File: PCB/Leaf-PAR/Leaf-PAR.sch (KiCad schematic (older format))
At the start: 3 parts

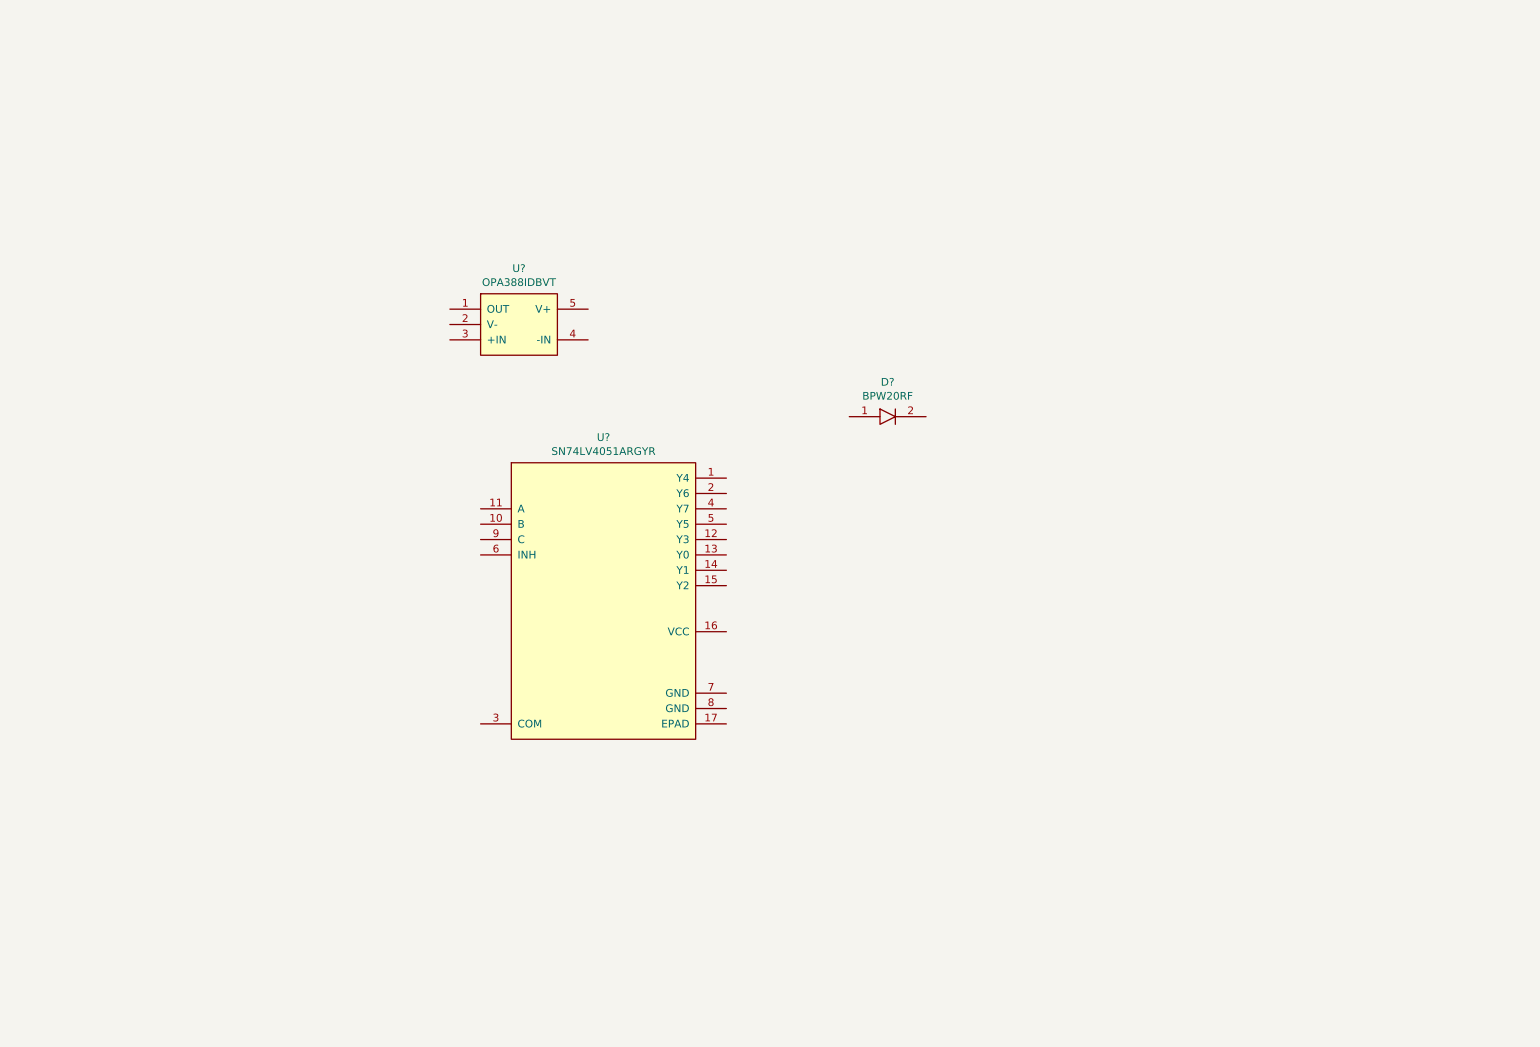
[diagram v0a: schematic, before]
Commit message: Schematic
Schematic pass 1 complete, next to add interface connector, need to decide if ADC or MCU should be integrated.
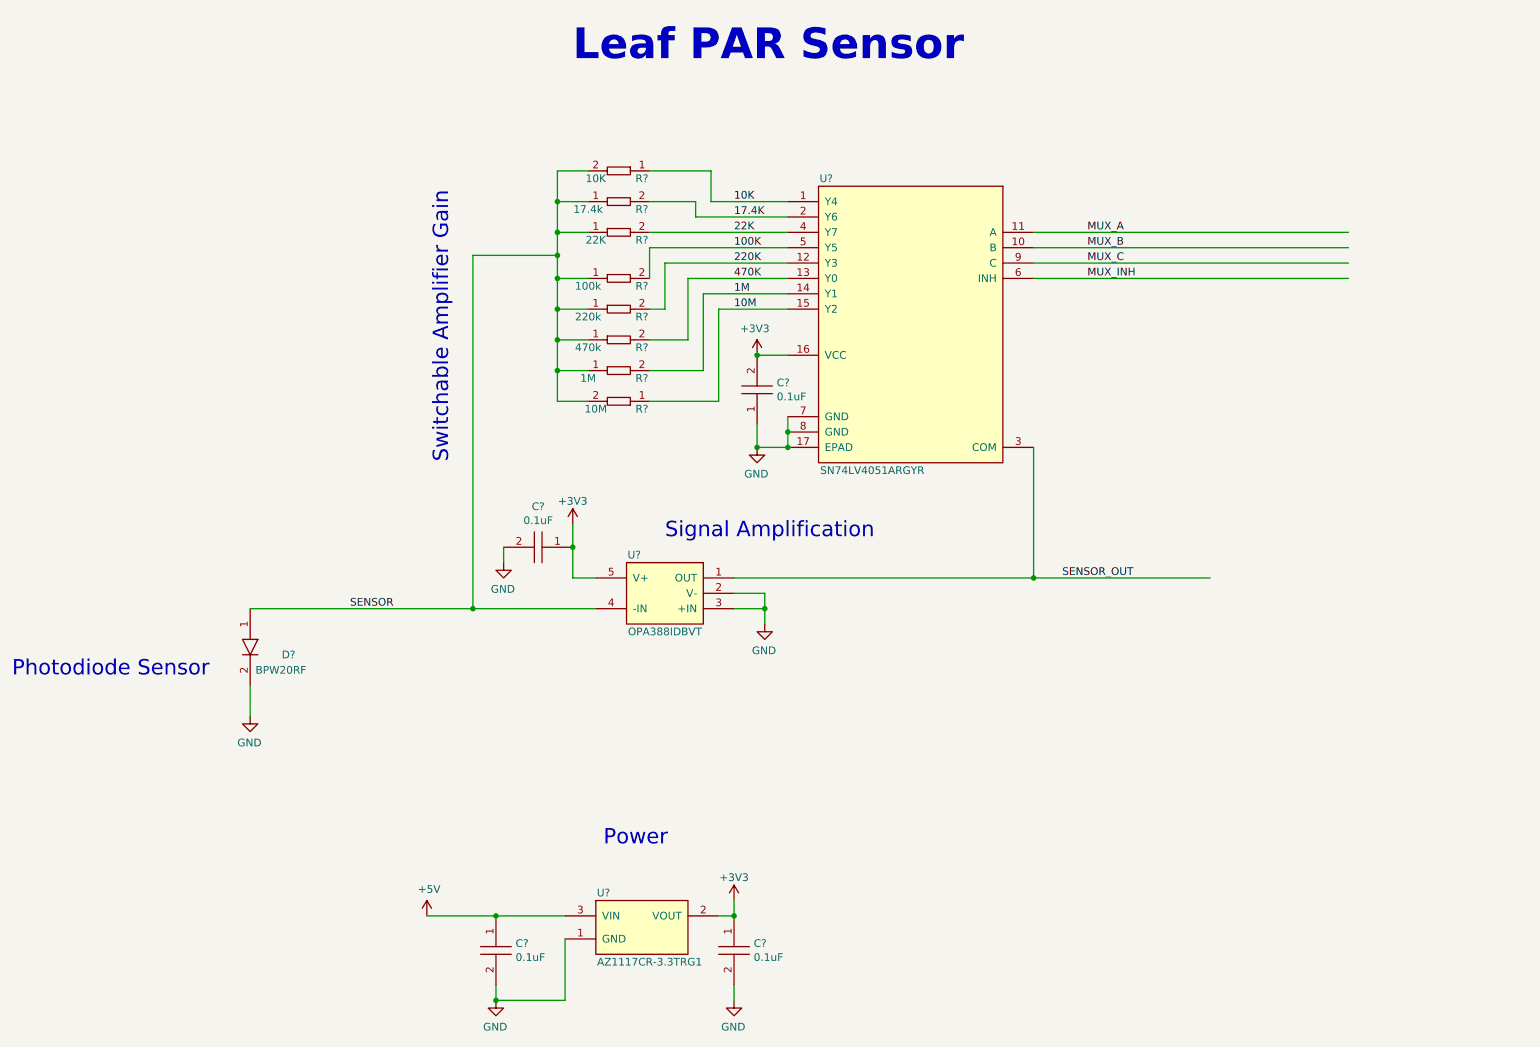
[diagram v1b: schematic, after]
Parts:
- added C? (x2): ECW-U1104JC9, AVR-KiCAD-Lib-Capacitors:ECW-U1104JC9, symbol AVR-KiCAD-Lib-Capacitors:ECW-U1104JC9
- added C?: C0402C104K9PACTU, AVR-KiCAD-Lib-Resistors:R0402, symbol AVR-KiCAD-Lib-Capacitors:C0402C104K9PACTU
- added C?: CGA3E2X7R1H104K080AA, AVR-KiCAD-Lib-Capacitors:C0603, symbol AVR-KiCAD-Lib-Capacitors:CGA3E2X7R1H104K080AA
- added R?: RC0402FR-0710KL, AVR-KiCAD-Lib-Resistors:R0402, symbol AVR-KiCAD-Lib-Resistors:RC0402FR-0710KL
- added R?: RT0402FRE0722KL, AVR-KiCAD-Lib-Resistors:R0402, symbol AVR-KiCAD-Lib-Resistors:RT0402FRE0722KL
- added R?: RC0402FR-0717K4L, AVR-KiCAD-Lib-Resistors:R0402, symbol AVR-KiCAD-Lib-Resistors:RC0402FR-0717K4L
- added R?: RC0402FR-07100KL, AVR-KiCAD-Lib-Resistors:R0402, symbol AVR-KiCAD-Lib-Resistors:RC0402FR-07100KL
- added R?: AC0402FR-07220KL, AVR-KiCAD-Lib-Resistors:R0402, symbol AVR-KiCAD-Lib-Resistors:AC0402FR-07220KL
- added R?: AC0402FR-07470KL, AVR-KiCAD-Lib-Resistors:R0402, symbol AVR-KiCAD-Lib-Resistors:AC0402FR-07470KL
- added R?: RC0402FR-071ML, AVR-KiCAD-Lib-Resistors:R0402, symbol AVR-KiCAD-Lib-Resistors:RC0402FR-071ML
- added R?: RC0402FR-0710ML, AVR-KiCAD-Lib-Resistors:R0402, symbol AVR-KiCAD-Lib-Resistors:RC0402FR-0710ML
- added U?: AZ1117CR-3.3TRG1, AVR-KiCAD-Lib-ICs:SOT_89, symbol AVR-KiCAD-Lib-ICs:AZ1117CR-3.3TRG1
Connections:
- net labels added: +3V3, +5V, 100K, 10K, 10M, 17.4K, 1M, 220K, 22K, 470K, GND, MUX_A, MUX_B, MUX_C, MUX_INH, SENSOR, SENSOR_OUT
- wire segments 0 -> 70
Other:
- note added: "Leaf PAR Sensor"
- note added: "Photodiode Sensor"
- note added: "Power"
- note added: "Signal Amplification"
- note added: "Switchable Amplifier Gain"
- moved on the sheet: D?, U?

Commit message: PCB
PCB first pass designed, pending review before proto
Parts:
- removed C?: ECW-U1104JC9, AVR-KiCAD-Lib-Capacitors:ECW-U1104JC9, symbol AVR-KiCAD-Lib-Capacitors:ECW-U1104JC9
- removed C?: C0402C104K9PACTU, AVR-KiCAD-Lib-Resistors:R0402, symbol AVR-KiCAD-Lib-Capacitors:C0402C104K9PACTU
- added C3, C4: C0805C104M5RACTU, AVR-KiCAD-Lib-Capacitors:C0805, symbol AVR-KiCAD-Lib-Capacitors:C0805C104M5RACTU
- added T1: PPTC081LFBN-RC, AVR-KiCAD-Lib-Connectors:Female_Header_Straight_1x08_Pitch2.54mm, symbol AVR-KiCAD-Lib-Connectors:PPTC081LFBN-RC
- gave numbers to parts that had none: 14
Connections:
- wire segments 70 -> 75
